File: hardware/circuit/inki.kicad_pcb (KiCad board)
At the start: 2 copper layers, 47.2 x 55.5 mm, 40 parts, among them J1 connector epaper, J2 Conn_01x02_Socket, J3 Conn_01x02_Socket, J4 Conn_01x02_Socket, J5 Conn_01x02_Socket, J7 Conn_01x02_Socket, Q1 TSM260P02CX, Q2 MMBT3904, Q3 IRLML6344TRPBF, SW1 SW_DIP_x04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

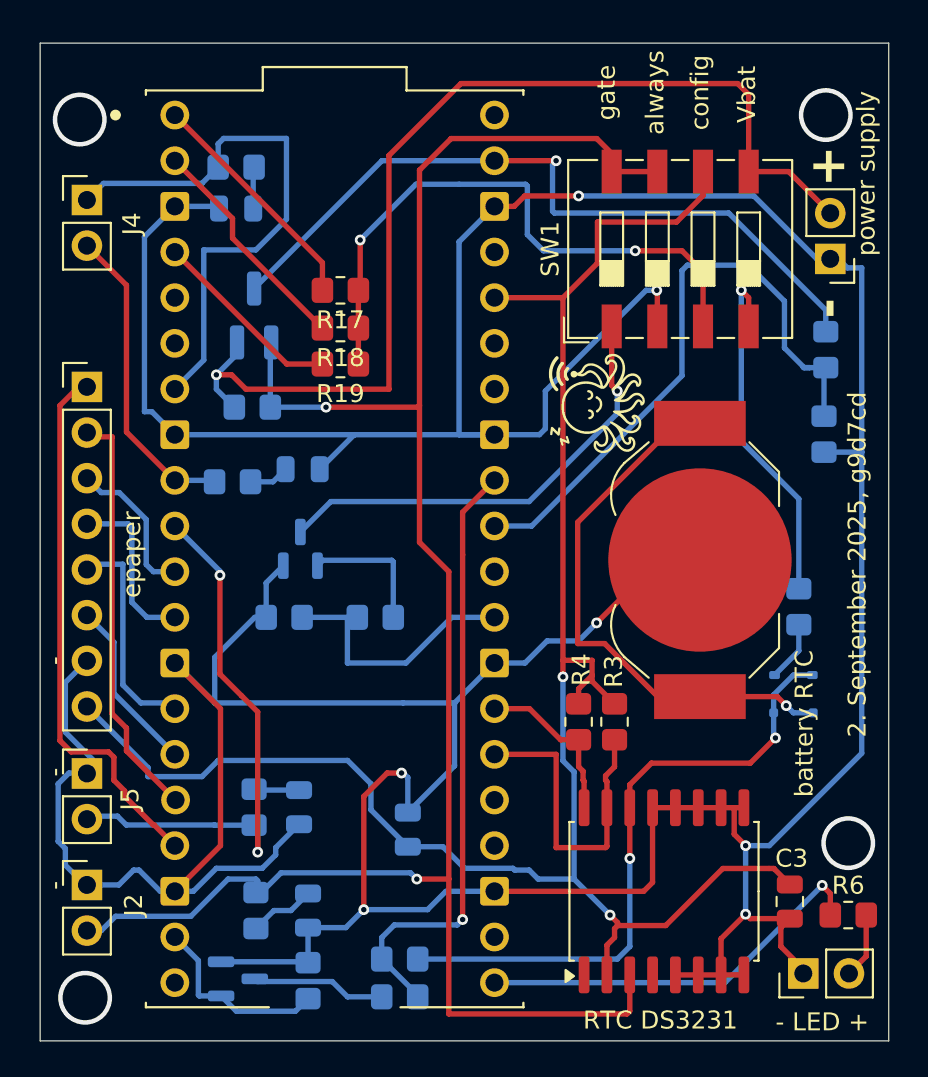
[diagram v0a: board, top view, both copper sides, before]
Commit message: modified pcb (all smds to one side), weathermap work
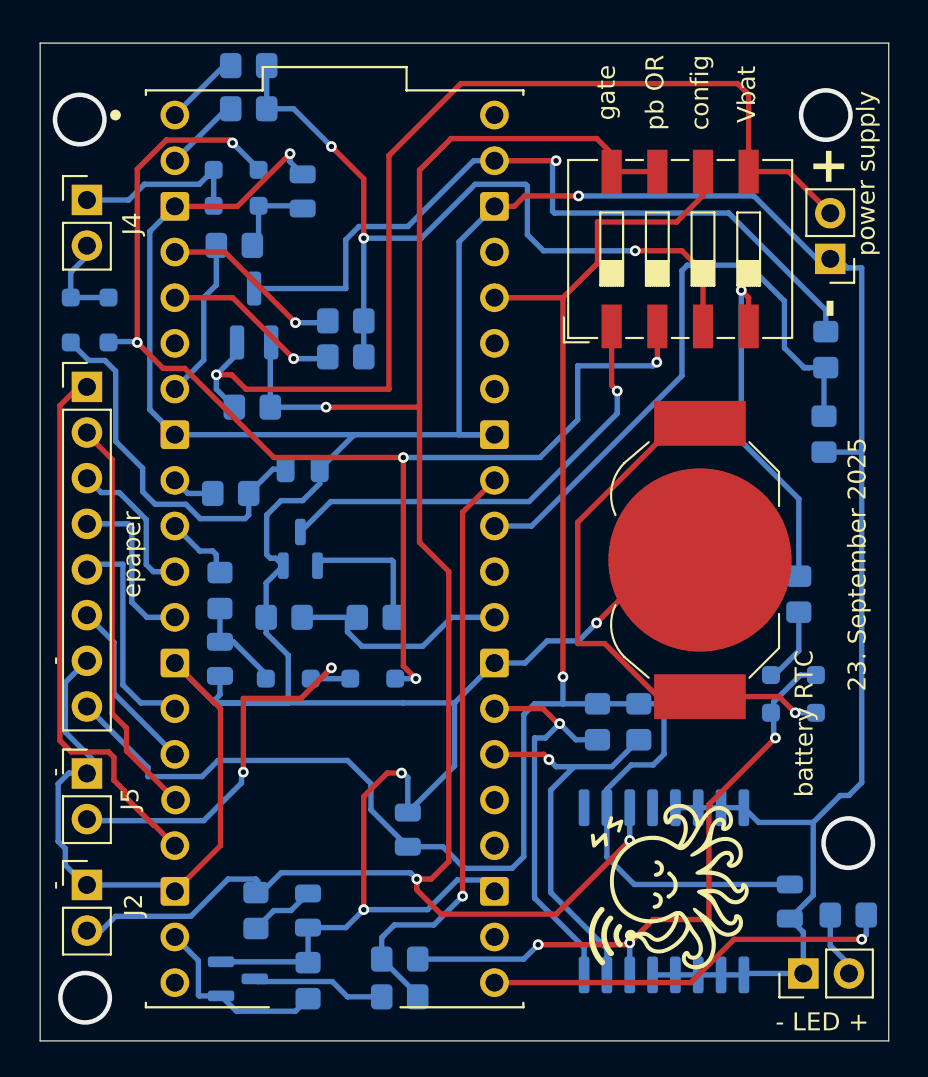
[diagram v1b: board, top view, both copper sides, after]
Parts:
- added D3: BAT54J, Diode_SMD:D_SOD-323_HandSoldering, B.Cu at (29.2, 50.0)
- added D4: BAT54J, Diode_SMD:D_SOD-323_HandSoldering, B.Cu at (33.9, 50.0)
- added D5: BAT54J, Diode_SMD:D_SOD-323_HandSoldering, B.Cu at (19.2, 30.1)
- added D6: BAT54J, Diode_SMD:D_SOD-323_HandSoldering, B.Cu at (17.1, 30.1)
- added D7: BAT54J, Diode_SMD:D_SOD-323_HandSoldering, B.Cu at (26.3, 21.7)
- added D8: BAT54J, Diode_SMD:D_SOD-323_HandSoldering, B.Cu at (26.3, 23.7)
- added R20: 10k, Resistor_SMD:R_0805_2012Metric_Pad1.20x1.40mm_HandSolder, B.Cu at (32.4, 32.1)
- C3, R17, R18, R19, R3, R4, R6, U1: moved to B.Cu
- D1: footprint Diode_SMD:D_SOD-323F -> Diode_SMD:D_SOD-323_HandSoldering
- D2: footprint Diode_SMD:D_SOD-323 -> Diode_SMD:D_SOD-323_HandSoldering
- moved R17 13.5 mm to (27.0, 15.9)
- moved R18 13.2 mm to (27.0, 18.3)
- moved R13 12.2 mm to (25.4, 45.1)
- moved 100n4 9.35 mm to (25.4, 48.9)
- moved R11 4.35 mm to (26.2, 25.9), turned to 0 degrees
- moved 100n2 3.82 mm to (30.0, 22.9), turned to 90 degrees
- moved R19 2.42 mm to (32.4, 30.1)
- moved R3 1.35 mm to (48.7, 52.4)
- moved R4 1.05 mm to (46.4, 52.4)
- moved R16 0.70 mm to (57.6, 45.3)
- moved R12 0.66 mm to (26.0, 39.7), turned to 0 degrees
- turned R6 to 180 degrees
- turned U1 to -90 degrees
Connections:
- 100n2 pad 1: Net-(100n2-Pad1) -> Net-(D8-A)
- 100n3 pad 1: Net-(100n3-Pad1) -> Net-(D6-A)
- 100n4 pad 1: Net-(100n4-Pad1) -> Net-(D3-A)
- J4 pad 1: Net-(J4-Pin_1) -> Net-(D7-K)
- J4 pad 2: Net-(J4-Pin_2) -> Net-(D5-K)
- J5 pad 2: Net-(J5-Pin_2) -> Net-(D3-K)
- R11 pad 1: Net-(100n2-Pad1) -> Net-(pico1-GP5)
- R11 pad 2: Net-(J4-Pin_1) -> Net-(D8-A)
- R12 pad 1: Net-(100n3-Pad1) -> Net-(pico1-GP6)
- R12 pad 2: Net-(J4-Pin_2) -> Net-(D6-A)
- R13 pad 1: Net-(100n4-Pad1) -> Net-(pico1-GP7)
- R13 pad 2: Net-(J5-Pin_2) -> Net-(D3-A)
- SW1 pad 2: GND -> Net-(D4-A)
- pico1 pad 10: Net-(J5-Pin_2) -> Net-(pico1-GP7)
- pico1 pad 5: unconnected-(pico1-GP3-Pad5) -> Net-(pico1-GP3)
- pico1 pad 7: Net-(J4-Pin_1) -> Net-(pico1-GP5)
- pico1 pad 9: Net-(J4-Pin_2) -> Net-(pico1-GP6)
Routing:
- net Net-(D4-A): track 0.00 -> 70.7 mm, vias 0 -> 5
- net Net-(J4-Pin_1): track 31.5 -> 0.00 mm
- net Net-(J5-Pin_2): track 31.3 -> 0.00 mm, vias 2 -> 0
- net Net-(D3-K): track 0.00 -> 23.7 mm, vias 0 -> 2
- net GND: track 292.2 -> 270.3 mm, vias 7 -> 5
- net Net-(D6-A): track 0.00 -> 20.9 mm
- net Net-(J4-Pin_2): track 17.3 -> 0.00 mm
- net Net-(U1-SCL): track 9.30 -> 22.5 mm, vias 0 -> 1
- net Net-(R17-Pad1): track 33.9 -> 46.1 mm, vias 2 -> 3
- net Net-(pico1-GP3): track 0.00 -> 9.96 mm, vias 0 -> 1
- net Net-(D7-K): track 0.00 -> 9.74 mm
- net Net-(pico1-GP5): track 0.00 -> 8.95 mm
- net Net-(pico1-GP0): track 13.2 -> 4.25 mm
- net Net-(pico1-GP1): track 12.7 -> 4.31 mm
- net Net-(D3-A): track 0.00 -> 5.40 mm
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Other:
- board text added: "23. September 2025"
- board text added: "pb OR"
- board text removed: "2. September 2025, g9d7cd"
- board text removed: "always"
